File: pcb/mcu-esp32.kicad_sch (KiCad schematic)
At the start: 10 parts, among them Q6 BSS138, U10 ESP32-S3-WROOM-1-N8R8

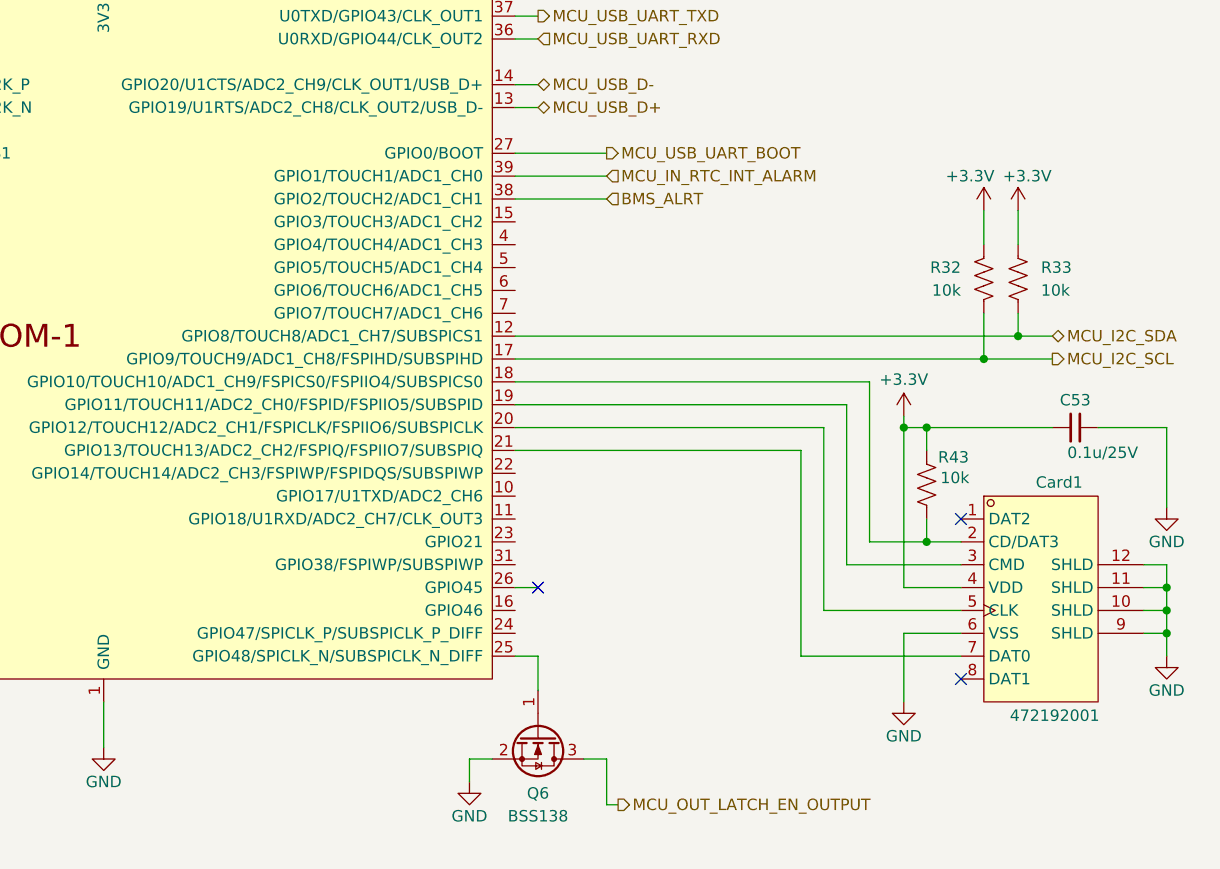
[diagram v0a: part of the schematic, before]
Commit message: Fix second mass-symbol-update reversion (recurred at same scale)
Same class of damage as the previous fix (commit 4ab9510) -- another
project-wide symbol resync reverted ~65 Datasheet fields and 5 Footprints
(Y2 crystal back to the wrong 5.0x3.2mm package again, U9/U12/U10/Y1
footprints back to non-stock equivalents) across all 7 schematic files.
Restored every field to its previously-verified value.

Also caught two real, independent bugs surfaced while re-checking (not
caused by this reversion, pre-existing): R32/R33/R43/R18 (10k YAGEO
RT0603BRD0710KL pull-ups, C95204) all had a mismatched Datasheet pointing
to a different resistor's PDF (RC0805FR-0710KL, wrong package family);
C36's Datasheet had drifted back to a different capacitor's PDF again
(same bug fixed once already this session).

ERC clean, same 14 pre-existing errors, no regressions.

Co-Authored-By: Claude Sonnet 5 <noreply@anthropic.com>
Claude-Session: https://claude.ai/code/session_01LhLkuH6sQ5GbUZ61bG7p2h
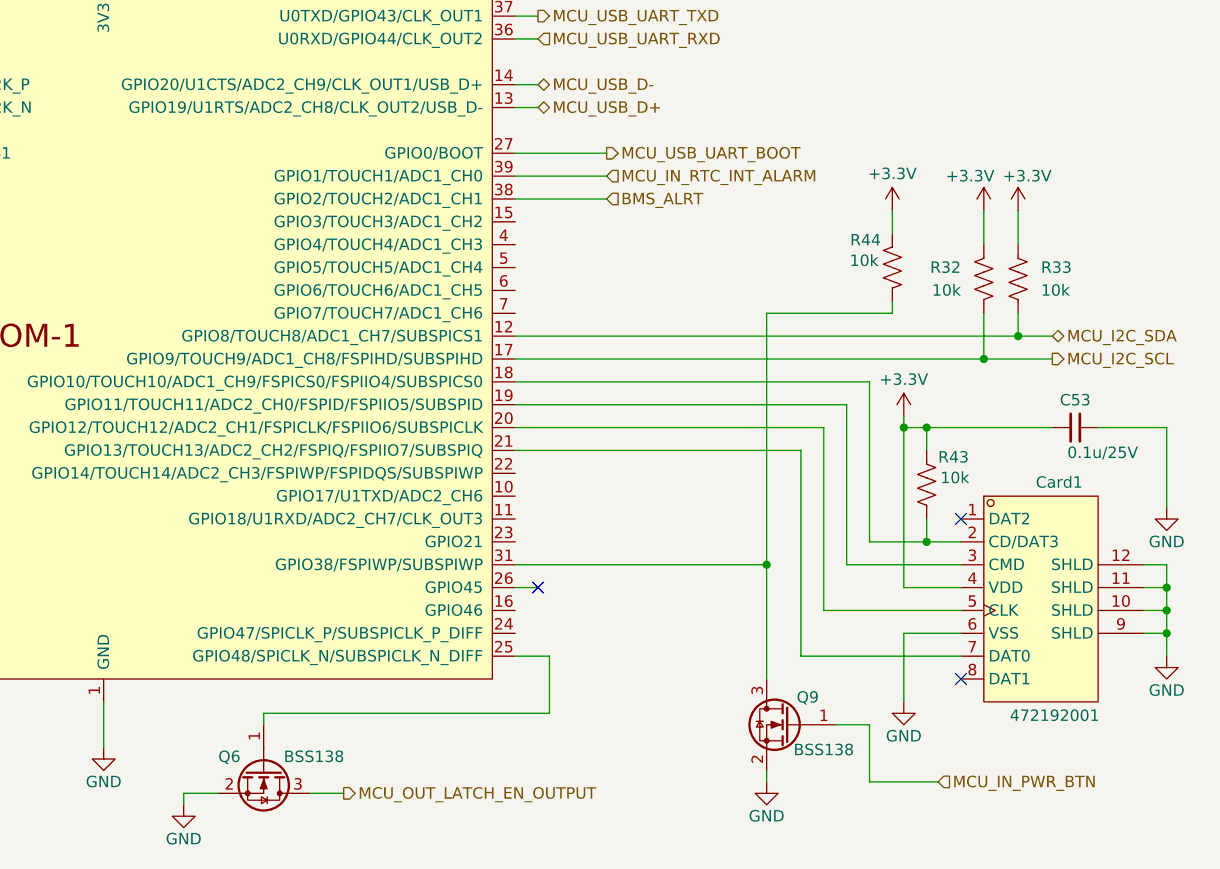
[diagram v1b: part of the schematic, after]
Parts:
- added Q9: BSS138, Package_TO_SOT_SMD:SOT-23, symbol Transistor_FET:BSS138
- added R44: 10k, Resistor_SMD:R_0603_1608Metric, symbol Device:R_US
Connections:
- net +3.3V: now also R44.2
- net GND: now also Q9.2 (S)
- net at U10.31 (GPIO38/FSPIWP/SUBSPIWP): now also Q9.3 (D), R44.1
- new net MCU_IN_PWR_BTN: Q9.1 (G)
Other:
- moved on the sheet: Q6

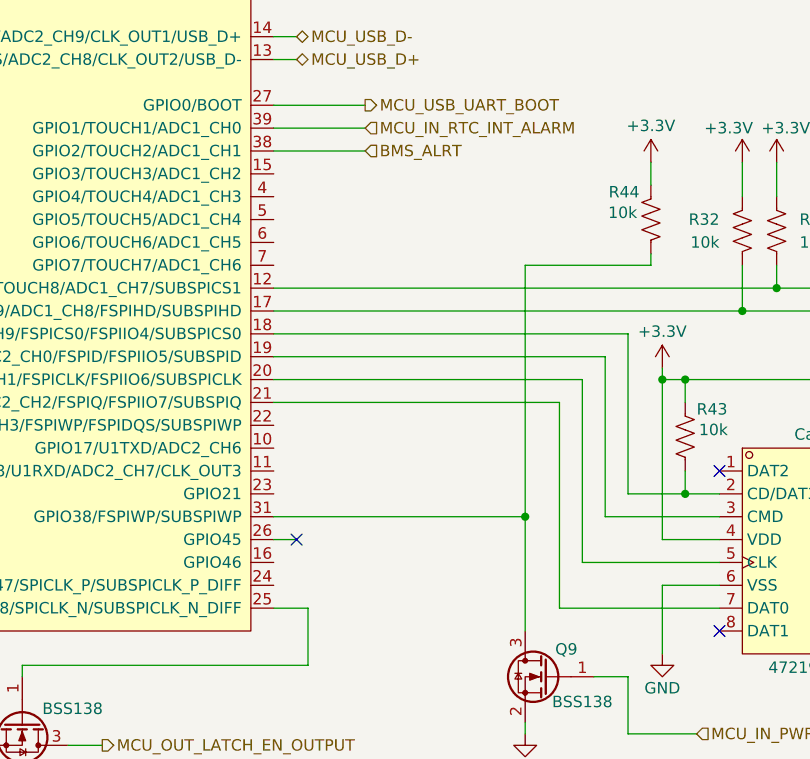
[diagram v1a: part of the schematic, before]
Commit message: Add I2S audio (PCM5102A) and GPS (MAX-M10S) schematic sheets
Audio: PCM5102A DAC with charge-pump network, per-channel output
filters, OUTL mic-level attenuator (divider + DC-block cap) for
SA818S/HT feed, OUTR spare-channel JST breakout, XSMT wired to the
board's last spare GPIO (GPIO3) for MCU-controlled muting.

GPS: MAX-M10S module, UART+PPS to ESP32-S3 (IO17/IO18/IO5), SMA RF
input with active-antenna bias-tee (bench through-hole SMA connector
for now, SMD swap planned), CR2032 holder placed (backup diode-OR
network not yet wired in).

Co-Authored-By: Claude Sonnet 5 <noreply@anthropic.com>
Claude-Session: https://claude.ai/code/session_01LhLkuH6sQ5GbUZ61bG7p2h
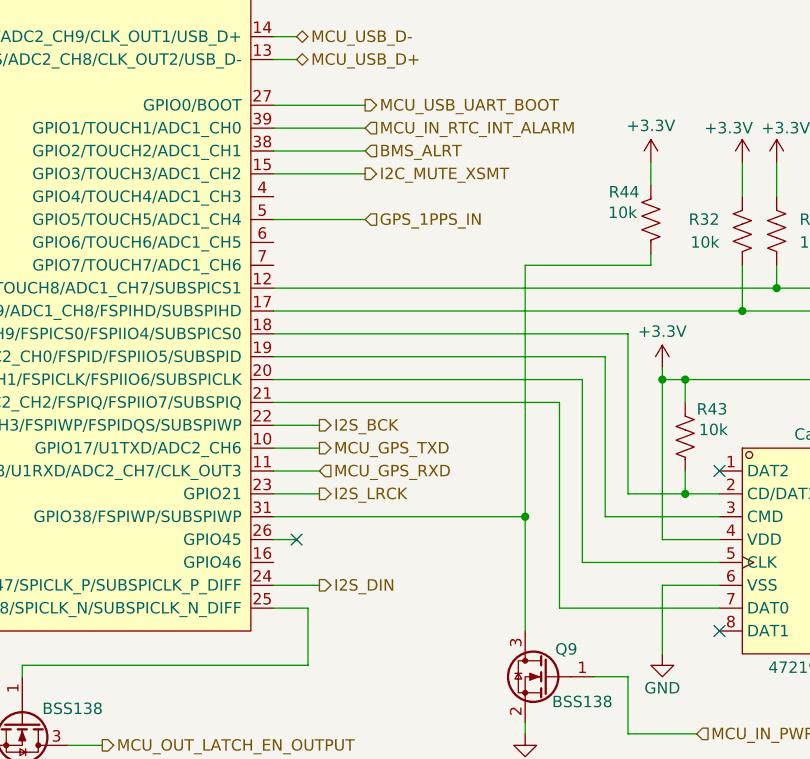
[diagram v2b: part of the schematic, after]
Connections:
- net MCU_GPS_TXD: now reaches U10.10 (GPIO17/U1TXD/ADC2_CH6)
- net MCU_GPS_RXD: now reaches U10.11 (GPIO18/U1RXD/ADC2_CH7/CLK_OUT3)
- net I2C_MUTE_XSMT: now reaches U10.15 (GPIO3/TOUCH3/ADC1_CH2)
- net I2S_BCK: now reaches U10.22 (GPIO14/TOUCH14/ADC2_CH3/FSPIWP/FSPIDQS/SUBSPIWP)
- net I2S_LRCK: now reaches U10.23 (GPIO21)
- net I2S_DIN: now reaches U10.24 (GPIO47/SPICLK_P/SUBSPICLK_P_DIFF)
- net GPS_1PPS_IN: now reaches U10.5 (GPIO5/TOUCH5/ADC1_CH4)
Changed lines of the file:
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@@
+	(wire
+		(pts
+			(xy 196.85 149.86) (xy 191.77 149.86)
+		)
+		(stroke
+			(width 0)
+			(type default)
+		)
+	)
 	(wire
 		(pts
@@
 	(wire
 		(pts
+			(xy 196.85 139.7) (xy 191.77 139.7)
+		)
+		(stroke
+			(width 0)
+			(type default)
+		)
+	)
+	(wire
+		(pts
 			(xy 231.14 139.7) (xy 231.14 121.92)
 		)
@@
 	(wire
 		(pts
+			(xy 191.77 109.22) (xy 201.93 109.22)
+		)
+		(stroke
+			(width 0)
+			(type default)
+		)
+	)
+	(wire
+		(pts
 			(xy 264.16 127) (xy 264.16 135.89)
 		)
@@
 	(wire
 		(pts
+			(xy 196.85 132.08) (xy 191.77 132.08)
+		)
+		(stroke
+			(width 0)
+			(type default)
+		)
+	)
+	(wire
+		(pts
 			(xy 191.77 88.9) (xy 194.31 88.9)
 		)
@@
 	(wire
 		(pts
+			(xy 191.77 134.62) (xy 196.85 134.62)
+		)
+		(stroke
+			(width 0)
+			(type default)
+		)
+	)
+	(wire
+		(pts
 			(xy 191.77 96.52) (xy 201.93 96.52)
 		)
@@
 	(wire
 		(pts
+			(xy 191.77 104.14) (xy 201.93 104.14)
+		)
+		(stroke
+			(width 0)
+			(type default)
+		)
+	)
+	(wire
+		(pts
 			(xy 237.49 137.16) (xy 237.49 139.7)
 		)
@@
 		(pts
 			(xy 154.94 167.64) (xy 158.75 167.64)
+		)
+		(stroke
+			(width 0)
+			(type default)
+		)
+	)
+	(wire
+		(pts
+			(xy 191.77 137.16) (xy 196.85 137.16)
 		)
 		(stroke
@@
 		)
 	)
+	(hierarchical_label "GPS_1PPS_IN"
+		(shape input)
+		(at 201.93 109.22 0)
+		(effects
+			(font
+				(size 1.27 1.27)
+			)
+			(justify left)
+		)
+	)
+	(hierarchical_label "I2S_BCK"
+		(shape output)
+		(at 196.85 132.08 0)
+		(effects
+			(font
+				(size 1.27 1.27)
+			)
+			(justify left)
+		)
+	)
 	(hierarchical_label "MCU_I2C_SDA"
 		(shape bidirectional)
@@
 		)
 	)
+	(hierarchical_label "I2S_LRCK"
+		(shape output)
+		(at 196.85 139.7 0)
+		(effects
+			(font
+				(size 1.27 1.27)
+			)
+			(justify left)
+		)
+	)
 	(hierarchical_label "MCU_USB_UART_TXD"
 		(shape output)
@@
 		)
 	)
+	(hierarchical_label "MCU_GPS_RXD"
+		(shape input)
+		(at 196.85 137.16 0)
+		(effects
+			(font
+				(size 1.27 1.27)
+			)
+			(justify left)
+		)
+	)
+	(hierarchical_label "I2S_DIN"
+		(shape output)
+		(at 196.85 149.86 0)
+		(effects
+			(font
+				(size 1.27 1.27)
+			)
+			(justify left)
+		)
+	)
 	(hierarchical_label "BMS_ALRT"
 		(shape input)
@@
 		)
 	)
+	(hierarchical_label "I2C_MUTE_XSMT"
+		(shape output)
+		(at 201.93 104.14 0)
+		(effects
+			(font
+				(size 1.27 1.27)
+			)
+			(justify left)
+		)
+	)
 	(hierarchical_label "MCU_USB_UART_RXD"
 		(shape input)
@@
 		)
 	)
+	(hierarchical_label "MCU_GPS_TXD"
+		(shape output)
+		(at 196.85 134.62 0)
+		(effects
+			(font
+				(size 1.27 1.27)
+			)
+			(justify left)
+		)
+	)

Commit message: Add external HT jack (J11) and PTT keying FET (Q10)
J11 (CUI/Same Sky SJ2-3593D-SMT-TR, switched TRS): tip and ring
switches auto-disconnect the onboard SA818S audio/PTT feeds the
instant something is plugged in. Q10 (BSS138) keys the shared PTT
node from GPIO16, with R53 (10k) pull-up holding it released by
default. Reviewed: T/TN and R/RN wiring both verified correct
against the jack's normalling behavior.

Co-Authored-By: Claude Sonnet 5 <noreply@anthropic.com>
Claude-Session: https://claude.ai/code/session_01LhLkuH6sQ5GbUZ61bG7p2h
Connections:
- net MCU_OUT_PTT: now reaches U10.9 (GPIO16/U0CTS/ADC2_CH5/XTAL_32K_N)
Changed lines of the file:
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@@
+	(wire
+		(pts
+			(xy 90.17 91.44) (xy 100.33 91.44)
+		)
+		(stroke
+			(width 0)
+			(type default)
+		)
+	)
 	(wire
 		(pts
@@
 		)
 	)
+	(hierarchical_label "MCU_OUT_PTT"
+		(shape output)
+		(at 90.17 91.44 180)
+		(effects
+			(font
+				(size 1.27 1.27)
+			)
+			(justify right)
+		)
+	)

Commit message: Add SA818S-V sheet, update GPS antenna connector, MCU GPIO reassignments
- New SA818S-V sheet (U19): UART/PTT/MIC_IN wired; VBAT, ANT, PD, H/L
  still open (see sa818_pinout.md).
- gps.kicad_sch: J10 swapped to Amphenol 132289 edge-launch SMD SMA
  (same part planned for the SA818 antenna connector).
- mcu-esp32.kicad_sch: SA818 UART on IO6/IO7, PTT on IO16 (direct FET
  drive via Q10, not the originally-planned AND-gate scheme).
- peripherals.kicad_sch: in-progress PCA9555 channel changes.

Co-Authored-By: Claude Sonnet 5 <noreply@anthropic.com>
Claude-Session: https://claude.ai/code/session_01LhLkuH6sQ5GbUZ61bG7p2h
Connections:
- net MCU_SA818_UART_TXD: now reaches U10.6 (GPIO6/TOUCH6/ADC1_CH5)
- net MCU_SA818_UART_RXD: now reaches U10.7 (GPIO7/TOUCH7/ADC1_CH6)
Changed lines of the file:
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@@
+	(wire
+		(pts
+			(xy 195.58 114.3) (xy 191.77 114.3)
+		)
+		(stroke
+			(width 0)
+			(type default)
+		)
+	)
 	(wire
 		(pts
@@
 		(pts
 			(xy 146.05 157.48) (xy 146.05 162.56)
+		)
+		(stroke
+			(width 0)
+			(type default)
+		)
+	)
+	(wire
+		(pts
+			(xy 195.58 111.76) (xy 191.77 111.76)
 		)
 		(stroke
@@
 		)
 	)
+	(hierarchical_label "MCU_SA818_UART_RXD"
+		(shape input)
+		(at 195.58 114.3 0)
+		(effects
+			(font
+				(size 1.27 1.27)
+			)
+			(justify left)
+		)
+	)
 	(hierarchical_label "GPS_1PPS_IN"
 		(shape input)
@@
 		)
 	)
+	(hierarchical_label "MCU_SA818_UART_TXD"
+		(shape output)
+		(at 195.58 111.76 0)
+		(effects
+			(font
+				(size 1.27 1.27)
+			)
+			(justify left)
+		)
+	)

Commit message: Wire SA818 PD/H-L and PTT opto, GPS power gating with bench bypass, RF detector groundwork
- SA818S-V: wire PD/H-L to PCA9555 expander outputs; swap PTT-keying FET
  for PC817 optocoupler isolation on the shared SA818S/external-HT PTT line
- GPS: add Q10 (AO3407A) high-side P-FET gating VCC+VCC_IO together for
  genuine hardware backup mode, driven via Q13 level-shifter from a new
  PCA9555 output (PERIPH_OUT_GPS_PWRON); add JP28 as a source-to-drain
  bench bypass across Q10 for unconditional power during bring-up; wire
  EXTINT to another PCA9555 output (PERIPH_OUT_GPS_EXTINT, pulled low by
  R57) to experiment with UART software-standby + external wake
- peripherals: reassign PCA9555 channels for the above plus SA818 PD/H-L
- audio/mcu-esp32: forward-power detector tap wiring groundwork
- docs: add vhf_matching_detector.md (matching network + RF detector BOM
  and layout), index it in _docs/README.md

Co-Authored-By: Claude Sonnet 5 <noreply@anthropic.com>
Claude-Session: https://claude.ai/code/session_01LhLkuH6sQ5GbUZ61bG7p2h
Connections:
- net MCU_IN_DIG_RF_DET: now reaches U10.34 (MTDI/GPIO41/CLK_OUT1)
- net MCU_ANALOG_RF_DET: now reaches U10.4 (GPIO4/TOUCH4/ADC1_CH3)
- no-connect marks 7 -> 8
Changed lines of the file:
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@@
+	)
+	(no_connect
+		(at 194.31 147.32)
 	)
 	(no_connect
@@
 	(wire
 		(pts
+			(xy 191.77 147.32) (xy 194.31 147.32)
+		)
+		(stroke
+			(width 0)
+			(type default)
+		)
+	)
+	(wire
+		(pts
 			(xy 96.52 147.32) (xy 100.33 147.32)
 		)
@@
 	(wire
 		(pts
+			(xy 90.17 101.6) (xy 100.33 101.6)
+		)
+		(stroke
+			(width 0)
+			(type default)
+		)
+	)
+	(wire
+		(pts
 			(xy 247.65 116.84) (xy 251.46 116.84)
 		)
@@
 		(pts
 			(xy 234.95 149.86) (xy 234.95 157.48)
+		)
+		(stroke
+			(width 0)
+			(type default)
+		)
+	)
+	(wire
+		(pts
+			(xy 201.93 106.68) (xy 191.77 106.68)
 		)
 		(stroke
@@
 		)
 	)
+	(hierarchical_label "MCU_ANALOG_RF_DET"
+		(shape input)
+		(at 201.93 106.68 0)
+		(effects
+			(font
+				(size 1.27 1.27)
+			)
+			(justify left)
+		)
+	)
 	(hierarchical_label "MCU_SA818_UART_RXD"
 		(shape input)
@@
 		)
 	)
+	(hierarchical_label "MCU_IN_DIG_RF_DET"
+		(shape input)
+		(at 90.17 101.6 180)
+		(effects
+			(font
+				(size 1.27 1.27)
+			)
+			(justify right)
+		)
+	)
